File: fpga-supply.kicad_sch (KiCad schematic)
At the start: 64 parts, among them U1 MPFS250T-FCVG484

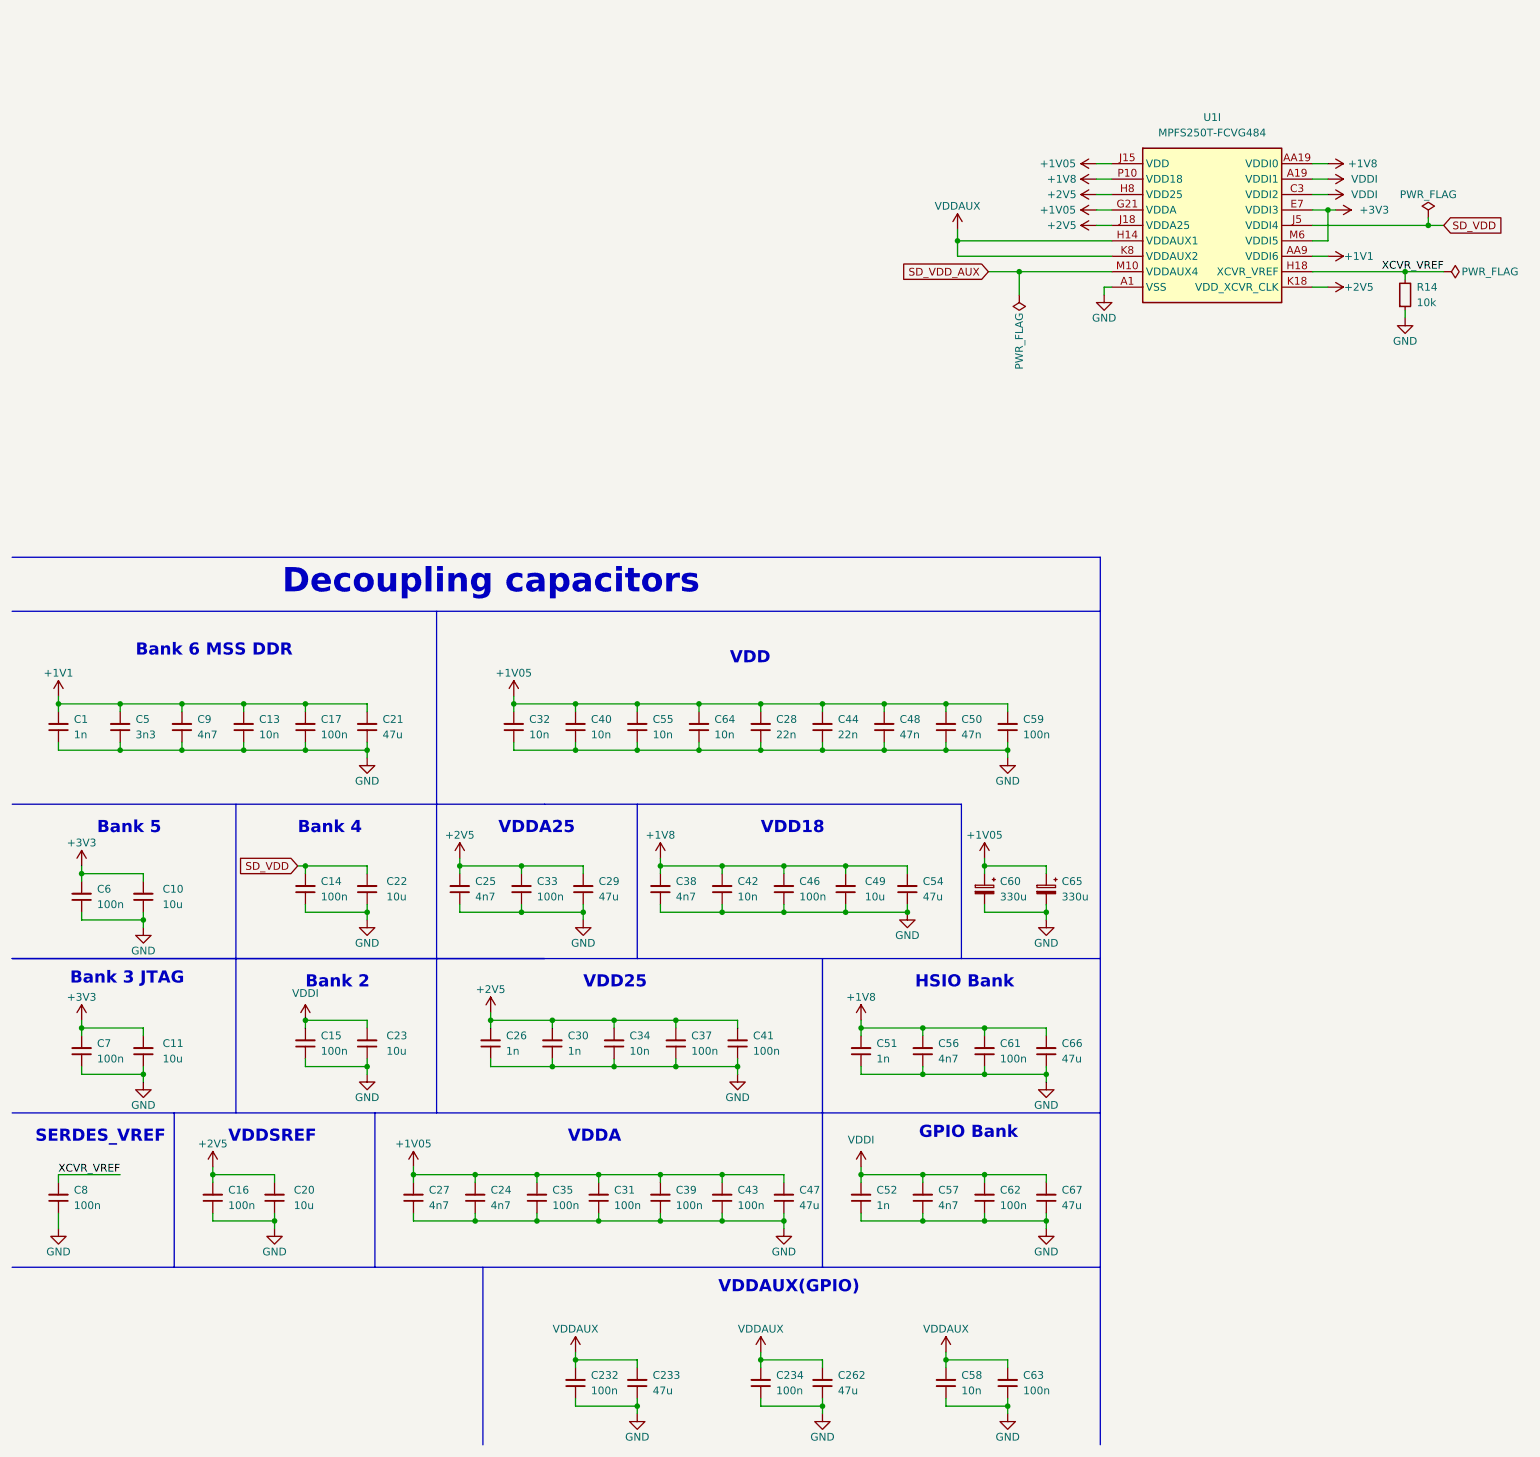
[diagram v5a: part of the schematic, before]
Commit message: [#57422] Align schematics
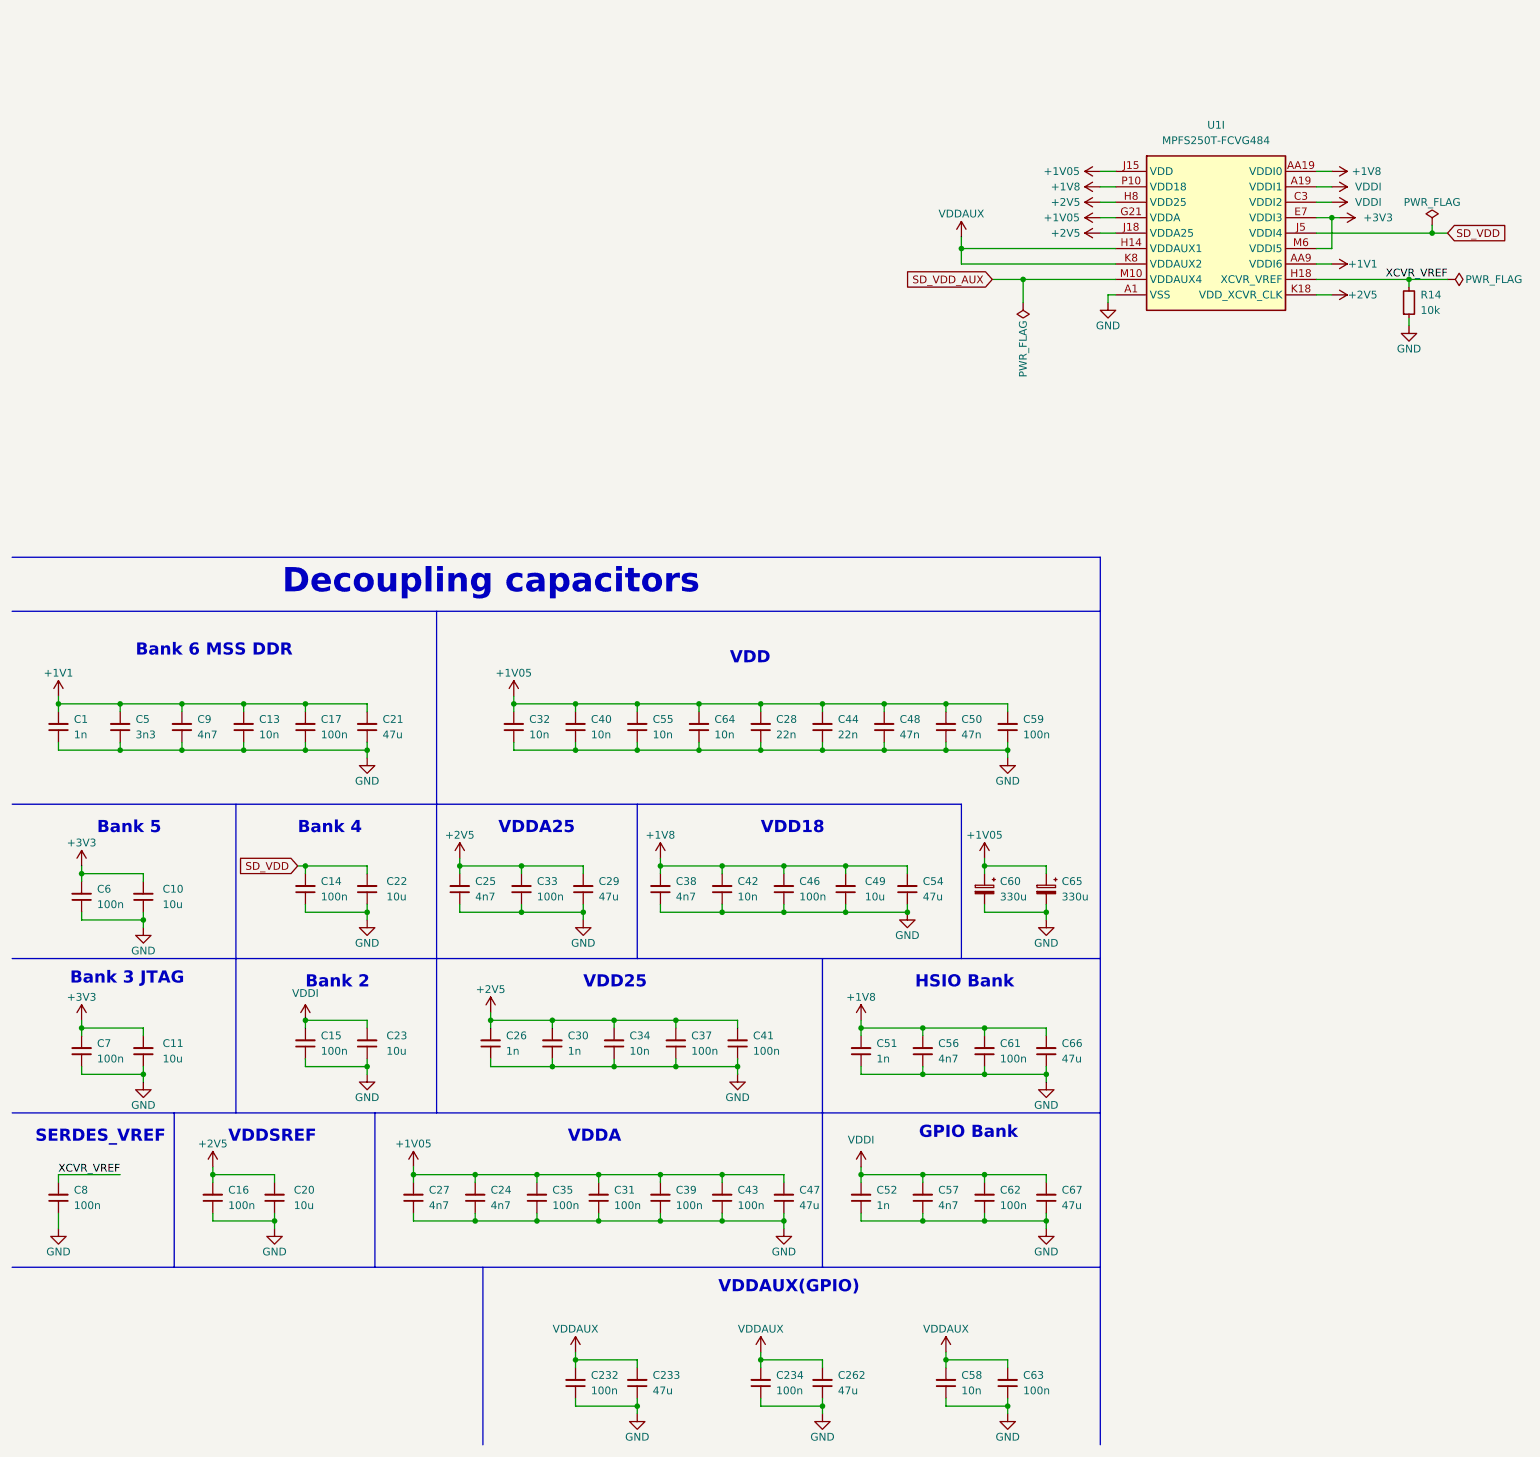
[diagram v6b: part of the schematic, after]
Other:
- moved on the sheet: R14, U1I
